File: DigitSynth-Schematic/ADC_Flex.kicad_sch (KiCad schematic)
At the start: 23 parts, among them J1 Conn_01x02_Pin, J2 Conn_01x02_Pin, J3 Conn_01x02_Pin, J4 Conn_01x02_Pin, U1 ADS1256IDBR

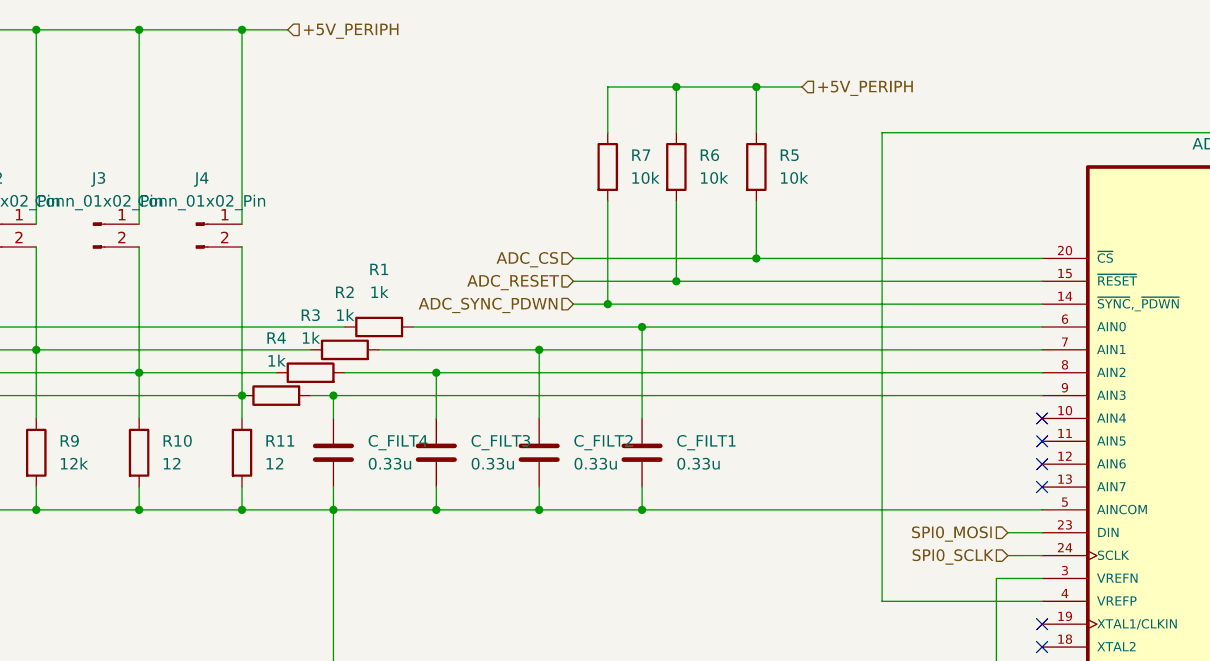
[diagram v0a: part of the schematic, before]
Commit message: removed power schematic sheet as RPI5 has decoupling capacitors; fixed component value errors; buttons removed from RPI5 sheet and added to ADC analog inputs; LED_VPLUS power line removed and replaced by +5V_PERIPH
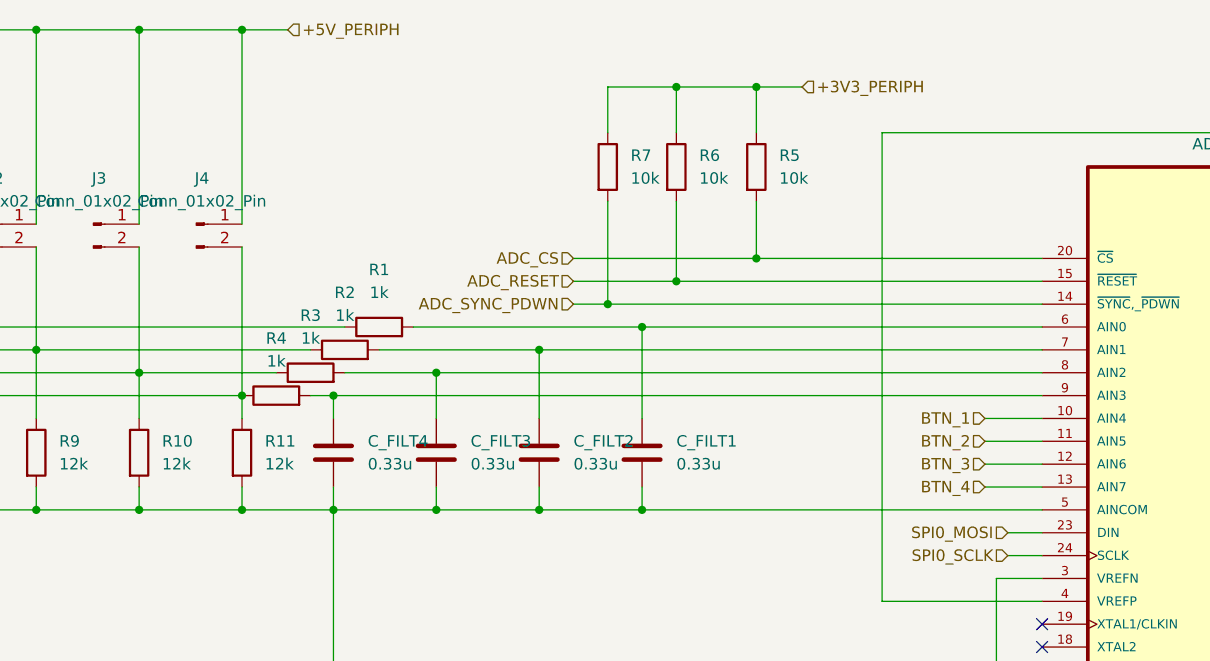
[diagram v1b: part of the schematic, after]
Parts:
- R10, R11: value 12 -> 12k
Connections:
- net +3V3_PERIPH: now also R5.1, R6.1, R7.1
- net +5V_PERIPH: no longer R5.1, R6.1, R7.1
- net BTN_1: now reaches U1.10 (AIN4)
- net BTN_2: now reaches U1.11 (AIN5)
- net BTN_3: now reaches U1.12 (AIN6)
- net BTN_4: now reaches U1.13 (AIN7)
- no-connect marks 10 -> 6
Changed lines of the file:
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@@
-	)
-	(no_connect
-		(at 165.1 66.04)
 	)
 	(no_connect
@@
 	)
 	(no_connect
-		(at 165.1 73.66)
-	)
-	(no_connect
 		(at 165.1 99.06)
 	)
@@
 	)
 	(no_connect
-		(at 165.1 71.12)
-	)
-	(no_connect
-		(at 165.1 68.58)
-	)
-	(no_connect
 		(at 165.1 104.14)
 	)
@@
 	(wire
 		(pts
+			(xy 158.75 68.58) (xy 165.1 68.58)
+		)
+		(stroke
+			(width 0)
+			(type default)
+		)
+	)
+	(wire
+		(pts
 			(xy 210.82 40.64) (xy 214.63 40.64)
 		)
@@
 	(wire
 		(pts
+			(xy 158.75 71.12) (xy 165.1 71.12)
+		)
+		(stroke
+			(width 0)
+			(type default)
+		)
+	)
+	(wire
+		(pts
 			(xy 86.36 76.2) (xy 76.2 76.2)
 		)
@@
 	(wire
 		(pts
+			(xy 158.75 66.04) (xy 165.1 66.04)
+		)
+		(stroke
+			(width 0)
+			(type default)
+		)
+	)
+	(wire
+		(pts
 			(xy 53.34 58.42) (xy 83.82 58.42)
 		)
@@
 		(pts
 			(xy 87.63 60.96) (xy 97.79 60.96)
+		)
+		(stroke
+			(width 0)
+			(type default)
+		)
+	)
+	(wire
+		(pts
+			(xy 158.75 73.66) (xy 165.1 73.66)
 		)
 		(stroke
@@
 		)
 	)
+	(hierarchical_label "BTN_3"
+		(shape input)
+		(at 158.75 71.12 180)
+		(effects
+			(font
+				(size 1.27 1.27)
+			)
+			(justify right)
+		)
+	)
 	(hierarchical_label "GND"
 		(shape input)
@@
 		)
 	)
-	(hierarchical_label "+5V_PERIPH"
+	(hierarchical_label "+3V3_PERIPH"
 		(shape input)
 		(at 138.43 29.21 0)
@@
 			)
 			(justify left)
+		)
+	)
+	(hierarchical_label "BTN_1"
+		(shape input)
+		(at 158.75 66.04 180)
+		(effects
+			(font
+				(size 1.27 1.27)
+			)
+			(justify right)
 		)
 	)
@@
 		(shape output)
 		(at 38.1 58.42 180)
+		(effects
+			(font
+				(size 1.27 1.27)
+			)
+			(justify right)
+		)
+	)
+	(hierarchical_label "BTN_4"
+		(shape input)
+		(at 158.75 73.66 180)
+		(effects
+			(font
+				(size 1.27 1.27)
+			)
+			(justify right)
+		)
+	)
+	(hierarchical_label "BTN_2"
+		(shape input)
+		(at 158.75 68.58 180)
 		(effects
 			(font
@@
 			)
 		)
-		(property "Value" "12"
+		(property "Value" "12k"
 			(at 78.74 71.1199 0)
 			(effects
@@
 			)
 		)
-		(property "Value" "12"
+		(property "Value" "12k"
 			(at 67.31 71.1199 0)
 			(effects

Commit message: updated schematic for PCB design
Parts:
- added TP1, TP2, TP3, TP4: TestPoint, symbol Connector:TestPoint
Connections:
- net AGND is gone; now on net GND: C_AVDD_1.2, C_AVDD_2.2, C_FILT1.2, C_FILT2.2, C_FILT3.2, C_FILT4.2, R10.2, R11.2, R8.2, R9.2, U1.2 (AGND), U1.3 (VREFN), U1.5 (AINCOM)
- net FLEX1_V: now also TP1.1
- net FLEX2_V: now also TP2.1
- net FLEX3_V: now also TP3.1
- net FLEX4_V: now also TP4.1
- net +3V3_PERIPH renamed +3V3_PI
- net +5V_PERIPH renamed +5V_PI
